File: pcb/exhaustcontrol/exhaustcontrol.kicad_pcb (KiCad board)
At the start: 2 copper layers, 55.9 x 36.8 mm, 15 parts, among them J1 Conn_01x03, J2 Conn_01x02, Q1 BC547, U1 74LS08

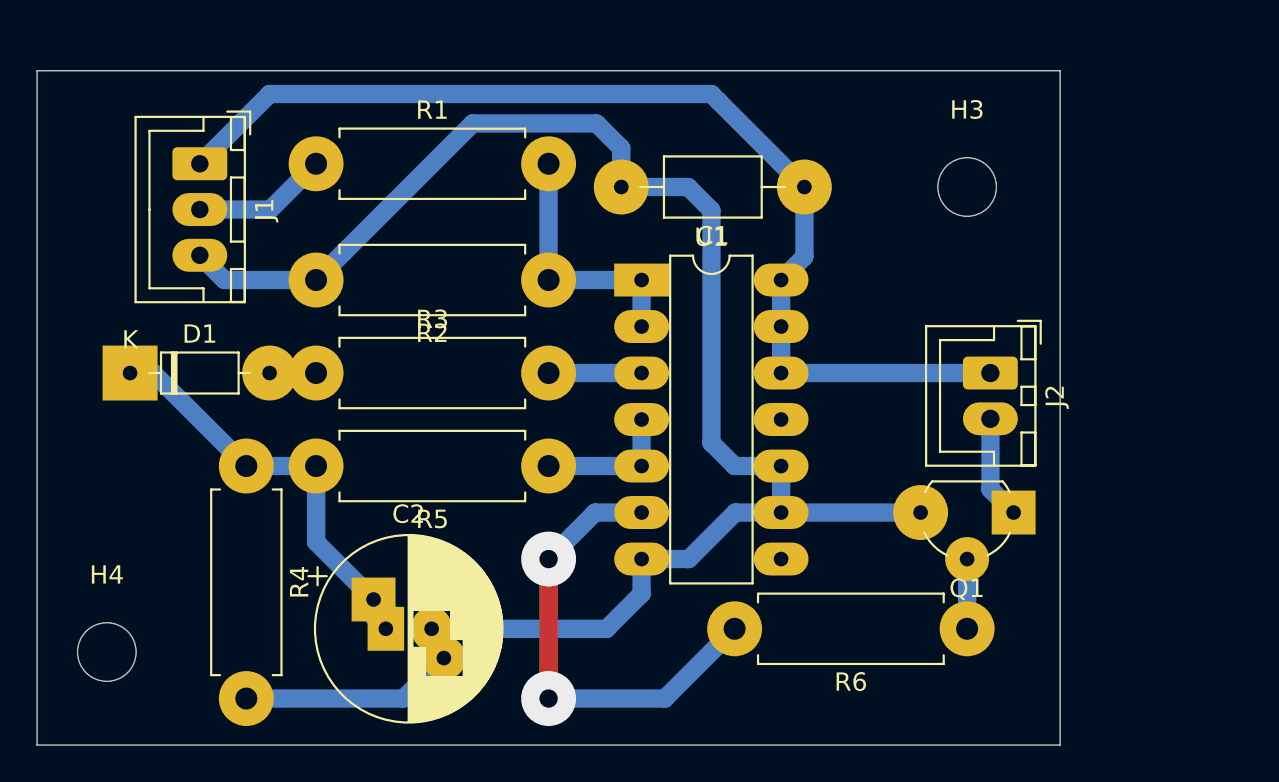
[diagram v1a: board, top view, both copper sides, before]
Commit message: Run SSR off 24 V.
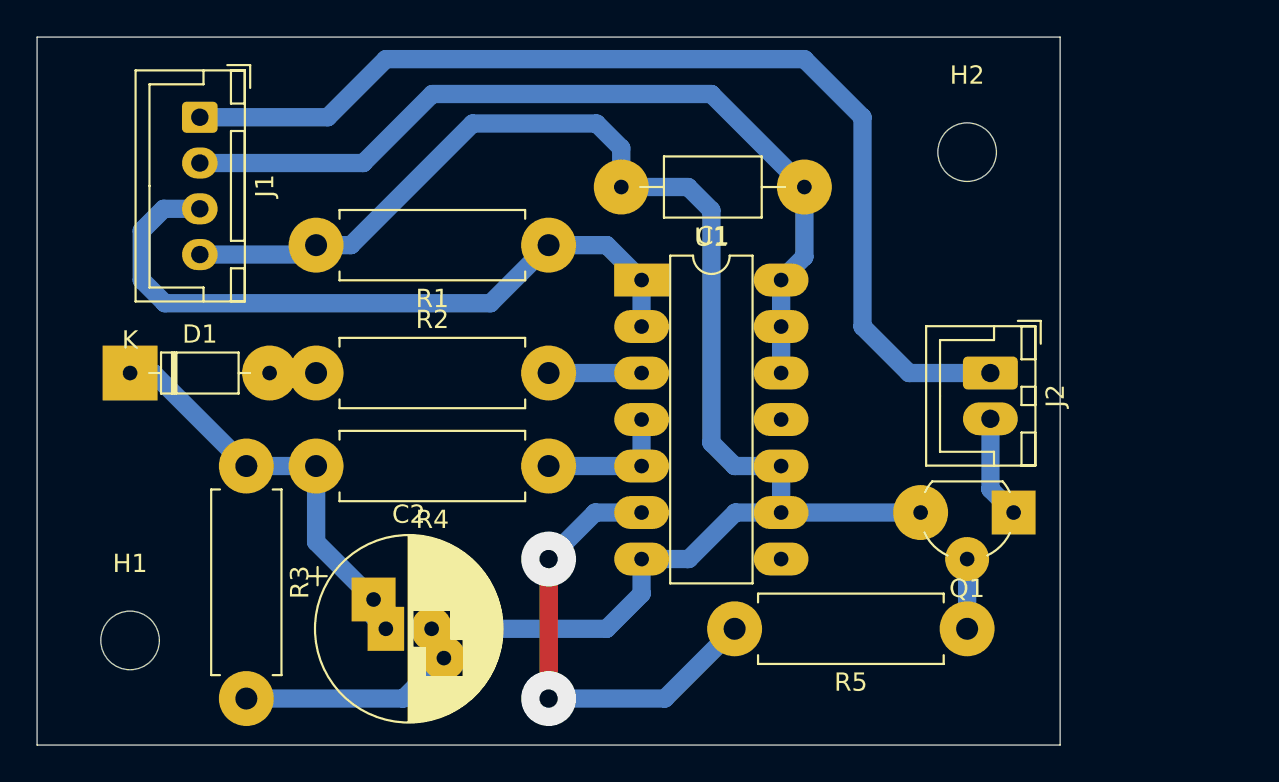
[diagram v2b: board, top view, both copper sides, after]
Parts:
- removed H3, H4: MountingHole, MountingHole:MountingHole_3.2mm_M3
- removed R6: 1k, Resistor_THT:R_Axial_DIN0411_L9.9mm_D3.6mm_P12.70mm_Horizontal
- added H1: MountingHole, MountingHole:MountingHole_3.2mm_M3, F.Cu at (97.8, 148.0)
- added H2: MountingHole, MountingHole:MountingHole_3.2mm_M3, F.Cu at (143.5, 121.3)
- C2: value 100u -> 220u
- J1: value Conn_01x03 -> JST XH; footprint Connector_JST:JST_XH_B03B-XH-A_1x03_P2.50mm_Vertical -> Connector_JST:JST_XH_B04B-XH-A_1x04_P2.50mm_Vertical
- R1: value 5k6 -> 4k7
- R2: value 1k -> 100
- R3: value 100 -> 1M
- R4: value 1M -> 1k
- U1: value 74LS08 -> 74HC08
- moved R5 24.5 mm to (143.5, 147.3)
- moved R4 16.5 mm to (120.7, 138.4), turned to 180 degrees
- moved R2 13.7 mm to (108.0, 133.3), turned to 0 degrees
- moved R1 13.5 mm to (120.7, 126.4), turned to 180 degrees
- moved R3 6.35 mm to (104.1, 138.4), turned to 270 degrees
- moved J1 2.54 mm to (101.6, 119.4)
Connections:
- J1 pad 1: +5V -> +24V
- J1 pad 2: Net-(J1-Pad2) -> +5V
- J1 pad 3: GND -> Net-(J1-Pad3)
- J2 pad 1: +5V -> +24V
- R1 pad 1: Net-(J1-Pad2) -> Net-(J1-Pad3)
- R1 pad 2: Net-(R1-Pad2) -> GND
- R2 pad 1: Net-(R1-Pad2) -> Net-(D1-Pad2)
- R2 pad 2: GND -> Net-(R2-Pad2)
- R3 pad 1: Net-(D1-Pad2) -> Net-(C2-Pad1)
- R3 pad 2: Net-(R3-Pad2) -> GND
- R4 pad 1: Net-(C2-Pad1) -> Net-(R4-Pad1)
- R4 pad 2: GND -> Net-(C2-Pad1)
- R5 pad 1: Net-(R5-Pad1) -> Net-(Q1-Pad2)
- R5 pad 2: Net-(C2-Pad1) -> Net-(R5-Pad2)
- U1 pad 1: Net-(R1-Pad2) -> Net-(J1-Pad3)
- U1 pad 2: Net-(R1-Pad2) -> Net-(J1-Pad3)
- U1 pad 3: Net-(R3-Pad2) -> Net-(R2-Pad2)
- U1 pad 4: Net-(R5-Pad1) -> Net-(R4-Pad1)
- U1 pad 5: Net-(R5-Pad1) -> Net-(R4-Pad1)
- U1 pad 6: Net-(R6-Pad2) -> Net-(R5-Pad2)
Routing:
- net +24V: track 0.00 -> 58.3 mm
- net Net-(J1-Pad3): track 0.00 -> 38.8 mm
- net Net-(R6-Pad2): track 25.5 -> 0.00 mm, vias 2 -> 0
- net Net-(R5-Pad2): track 0.00 -> 25.5 mm, vias 0 -> 2
- net Net-(R1-Pad2): track 14.0 -> 0.00 mm
- net +5V: track 58.8 -> 47.4 mm
- net Net-(R5-Pad1): track 7.62 -> 0.00 mm
- net Net-(R4-Pad1): track 0.00 -> 7.62 mm
- net Net-(J1-Pad2): track 7.39 -> 0.00 mm
- net Net-(R3-Pad2): track 5.08 -> 0.00 mm
- net Net-(R2-Pad2): track 0.00 -> 5.08 mm
- net GND: track 99.0 -> 97.8 mm
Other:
- board size 55.9 x 36.8 mm -> 55.9 x 38.7 mm

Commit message: Update to KiCad 5 format; add relay.
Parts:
- added K1: UMS05-1A80-75D, Exhaustcontrol:DIL-relay, F.Cu at (147.8, 125.7)
- Q1: footprint Package_TO_SOT_THT:TO-92L_Wide -> Package_TO_SOT_THT:TO-92_Wide
- moved J2 16.5 mm to (148.8, 149.4), turned to 0 degrees
- moved Q1 3.56 mm to (142.5, 141.0)
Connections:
- J2 pad 1: +24V -> Net-(J2-Pad1)
- J2 pad 2: Net-(J2-Pad2) -> GND
- Q1 pad 1: Net-(J2-Pad2) -> Net-(Q1-Pad1)
- U1 pad 11: Net-(U1-Pad11) -> unconnected-(U1-Pad11)
- U1 pad 8: Net-(U1-Pad8) -> unconnected-(U1-Pad8)
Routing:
- net +24V: track 58.3 -> 86.5 mm
- net GND: track 97.8 -> 121.7 mm
- net +5V: track 47.4 -> 70.7 mm
- net Net-(Q1-Pad1): track 0.00 -> 17.5 mm
- net Net-(J2-Pad1): track 0.00 -> 16.9 mm
- net Net-(J2-Pad2): track 5.65 -> 0.00 mm
- net Net-(Q1-Pad2): track 3.81 -> 5.28 mm
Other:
- board size 55.9 x 38.7 mm -> 64.5 x 38.6 mm
- net class Default removed
